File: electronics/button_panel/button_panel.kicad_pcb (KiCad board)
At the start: 2 copper layers, 31 parts, among them J1 Conn_01x10, J2 Conn_01x09, SW1 PWR, SW2 RST, SW3 AP, SW4 MAN, SW5 FC REC, SW6 USR1, SW7 USR2, SW8 USR3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

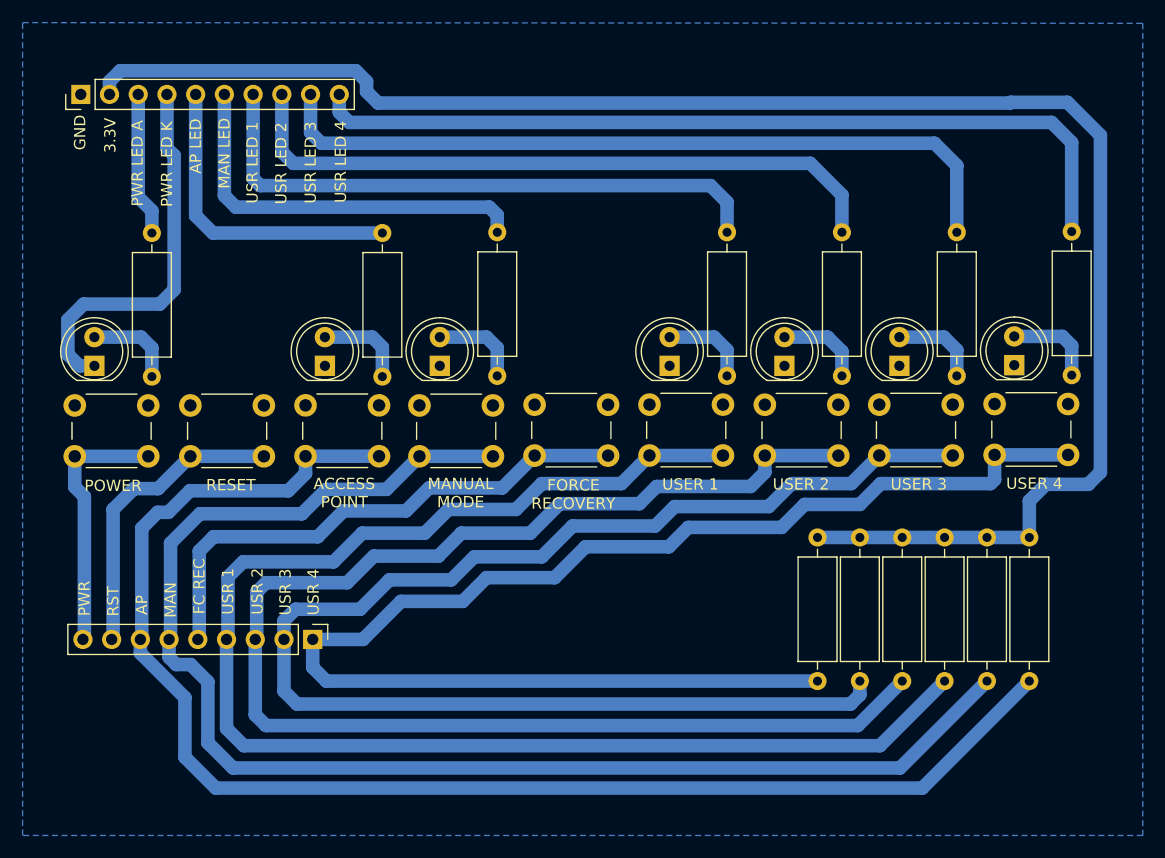
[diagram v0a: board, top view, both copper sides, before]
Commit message: Edit button panel, edit CAD, add motor tensioners
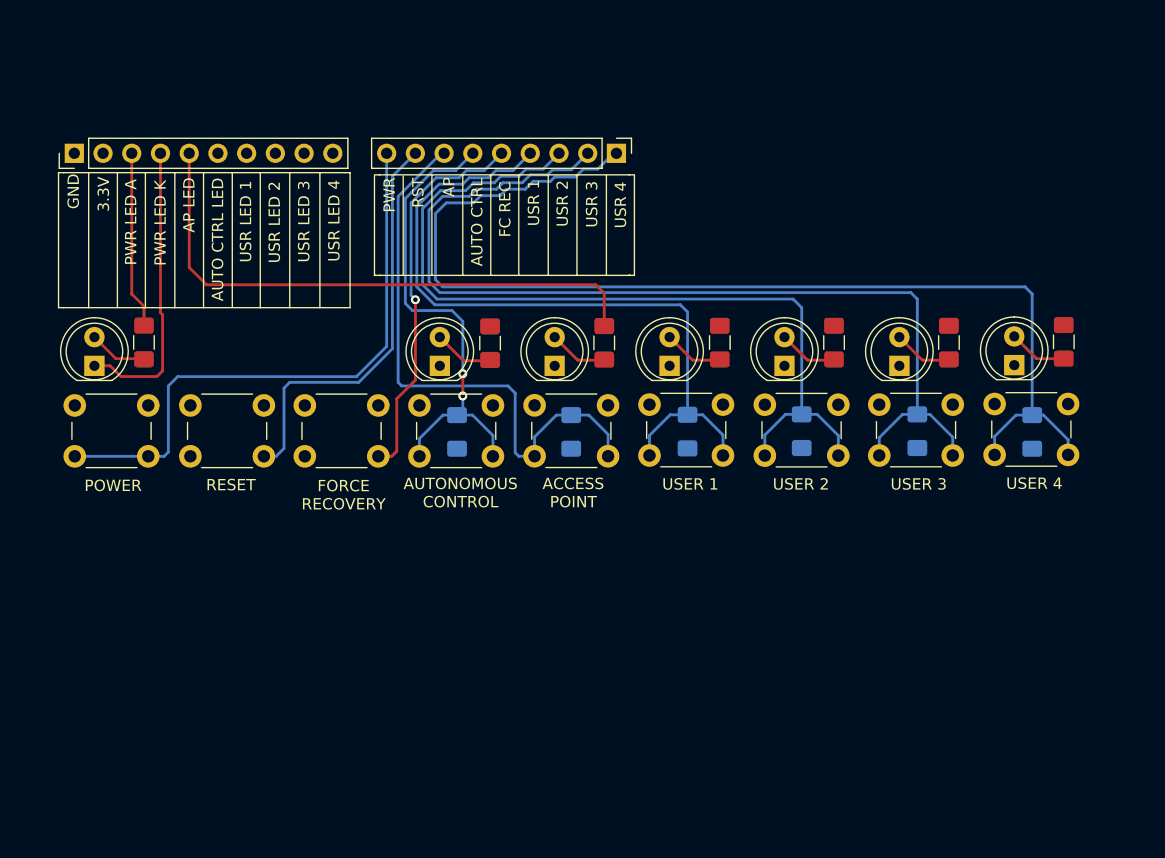
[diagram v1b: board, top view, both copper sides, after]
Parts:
- R1, R2, R3, R4, R7, R8, R9: footprint Resistor_THT:R_Axial_DIN0309_L9.0mm_D3.2mm_P12.70mm_Horizontal -> Resistor_SMD:R_1206_3216Metric_Pad1.42x1.75mm_HandSolder
- R10, R11, R12, R13, R5, R6: footprint Resistor_THT:R_Axial_DIN0309_L9.0mm_D3.2mm_P12.70mm_Horizontal -> Resistor_SMD:R_1206_3216Metric_Pad1.42x1.75mm_HandSolder; moved to B.Cu
- moved R6 51.8 mm to (150.0, 86.9), turned to 270 degrees
- moved J2 50.7 mm to (164.1, 62.3)
- moved R5 46.1 mm to (160.1, 86.9), turned to 270 degrees
- moved R13 31.7 mm to (170.4, 86.9), turned to 270 degrees
- moved R10 29.1 mm to (200.9, 86.9), turned to 270 degrees
- moved R12 23.8 mm to (180.5, 86.9), turned to 270 degrees
- moved R11 22.7 mm to (190.7, 86.9), turned to 270 degrees
- moved R3 21.9 mm to (163.0, 79.1)
- moved SW5 20.3 mm to (143.0, 89.1)
- moved D3 20.3 mm to (158.6, 81.1)
- moved SW3 20.3 mm to (163.3, 89.1)
- moved R2 9.83 mm to (152.9, 79.1)
- moved R7 9.78 mm to (193.5, 79.0)
- moved R8 9.78 mm to (183.3, 79.0)
- moved R1 9.78 mm to (203.6, 79.0)
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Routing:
- net +3V3: track 151.2 -> 0.00 mm
- net Net-(J2-Pad6): track 124.6 -> 42.7 mm, vias 0 -> 2
- net Net-(J1-Pad10): track 75.3 -> 0.00 mm
- net Net-(J2-Pad7): track 126.2 -> 51.6 mm
- net Net-(J1-Pad9): track 67.6 -> 0.00 mm
- net Net-(J2-Pad4): track 128.2 -> 64.6 mm
- net Net-(J1-Pad8): track 59.5 -> 0.00 mm
- net Net-(J1-Pad7): track 52.9 -> 0.00 mm
- net Net-(J2-Pad3): track 127.5 -> 76.3 mm
- net Net-(J2-Pad2): track 124.4 -> 87.9 mm
- net Net-(J1-Pad6): track 35.3 -> 0.00 mm
- net Net-(J2-Pad9): track 23.1 -> 52.1 mm
- net Net-(J2-Pad1): track 122.5 -> 99.2 mm
- net Net-(J1-Pad5): track 27.9 -> 50.6 mm
- net Net-(J2-Pad5): track 47.5 -> 34.4 mm, vias 0 -> 1
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- removed copper zone on B.Cu, net GND
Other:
- board text added: "AUTO CTRL"
- board text added: "AUTO CTRL LED"
- board text added: "AUTONOMOUS CONTROL"
- board text removed: "MAN"
- board text removed: "MAN LED"
- board text removed: "MANUAL MODE"

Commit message: Add chain guide models
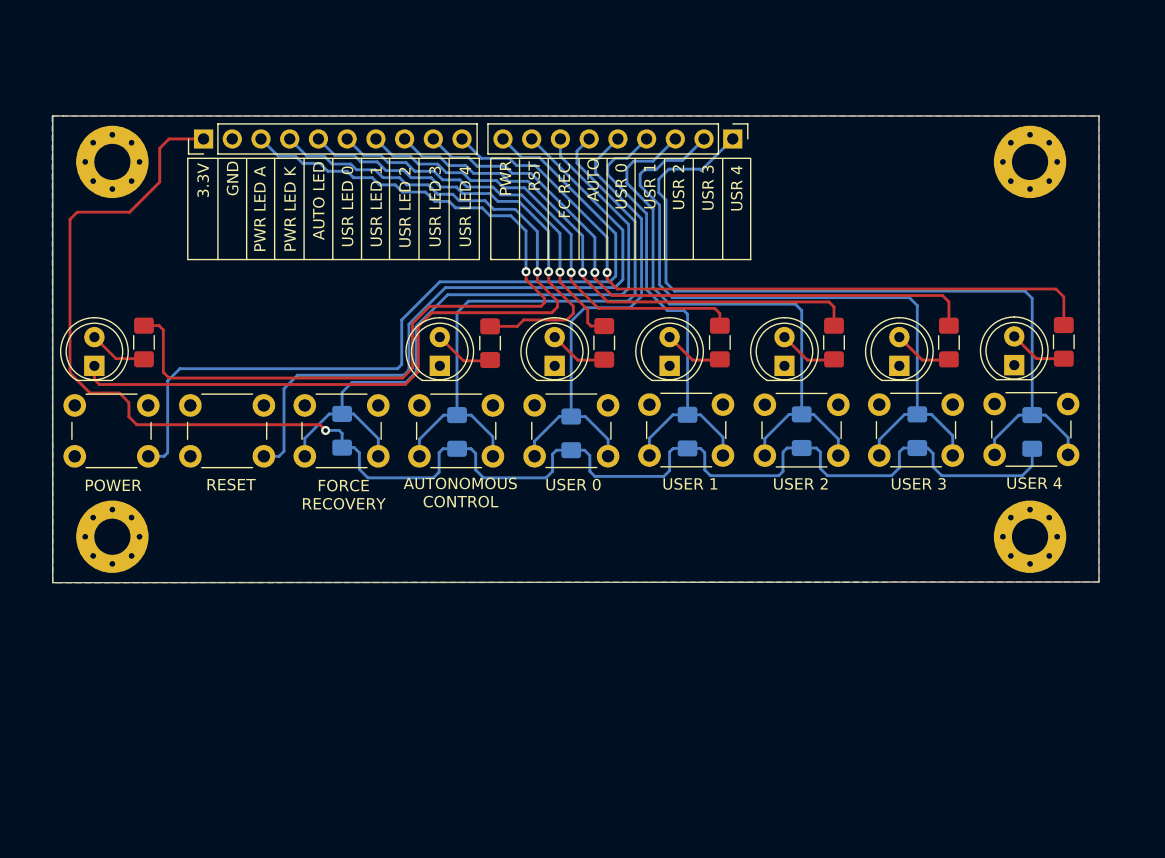
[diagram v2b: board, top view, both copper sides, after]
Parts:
- added R14: R, Resistor_SMD:R_1206_3216Metric_Pad1.42x1.75mm_HandSolder, B.Cu at (160.1, 87.1)
- added REF**: MountingHole_3.2mm_M3_Pad_Via, MountingHole:MountingHole_3.2mm_M3_Pad_Via, F.Cu at (200.7, 96.2)
- added REF**: MountingHole_3.2mm_M3_Pad_Via, MountingHole:MountingHole_3.2mm_M3_Pad_Via, F.Cu at (119.5, 96.2)
- added REF**: MountingHole_3.2mm_M3_Pad_Via, MountingHole:MountingHole_3.2mm_M3_Pad_Via, F.Cu at (200.7, 63.1)
- added REF**: MountingHole_3.2mm_M3_Pad_Via, MountingHole:MountingHole_3.2mm_M3_Pad_Via, F.Cu at (119.5, 63.1)
- D2, SW4: value MAN -> AUTO CTRL
- D3, SW3: value AP -> USR0
- moved R5 20.3 mm to (139.8, 86.8)
- moved J1 11.5 mm to (127.6, 61.0)
- moved J2 10.4 mm to (174.4, 61.0)
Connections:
- J1 pad 1: GND -> +3V3
- J1 pad 2: +3V3 -> GND
- R2 pad 1: Net-(J1-Pad6) -> Net-(J1-Pad5)
- R3 pad 1: Net-(J1-Pad5) -> Net-(J1-Pad6)
- SW3 pad 1: Net-(J2-Pad7) -> Net-(J2-Pad5)
- SW5 pad 1: Net-(J2-Pad5) -> Net-(J2-Pad7)
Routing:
- net +3V3: track 0.00 -> 142.2 mm, vias 0 -> 1
- net Net-(J1-Pad10): track 0.00 -> 63.6 mm, vias 0 -> 1
- net Net-(J1-Pad3): track 15.7 -> 78.4 mm, vias 0 -> 1
- net Net-(J1-Pad9): track 0.00 -> 55.8 mm, vias 0 -> 1
- net Net-(D4-Pad1): track 26.0 -> 80.2 mm, vias 0 -> 1
- net Net-(J1-Pad8): track 0.00 -> 47.9 mm, vias 0 -> 1
- net Net-(J1-Pad7): track 0.00 -> 40.3 mm, vias 0 -> 1
- net Net-(J1-Pad6): track 0.00 -> 32.8 mm, vias 0 -> 1
- net Net-(J2-Pad1): track 99.2 -> 71.9 mm
- net Net-(J2-Pad2): track 87.9 -> 62.0 mm
- net Net-(J2-Pad3): track 76.3 -> 51.3 mm
- net Net-(J2-Pad4): track 64.6 -> 41.5 mm
- net Net-(J2-Pad8): track 36.6 -> 59.6 mm
- net Net-(J2-Pad9): track 52.1 -> 71.2 mm
- net Net-(J1-Pad5): track 50.6 -> 39.7 mm, vias 0 -> 1
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- added copper zone on B.Cu, net GND
- added copper zone on F.Cu, net GND
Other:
- board outline added: 92.5 x 41.3 mm
- board text added: "AUTO"
- board text added: "AUTO LED"
- board text added: "USER 0"
- board text added: "USR 0"
- board text added: "USR LED 0"
- board text removed: "ACCESS POINT"
- board text removed: "AP"
- board text removed: "AP LED"
- board text removed: "AUTO CTRL"
- board text removed: "AUTO CTRL LED"
